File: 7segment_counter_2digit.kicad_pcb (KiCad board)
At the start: 2 copper layers, 68.6 x 94 mm, 14 parts, among them IC1 CD4026BE, IC2 CD4026BE, SW1 SW_Reset, SW2 SW_Count, U1 5611AH, U2 2462, U3 ICM7555, U4 5611AH

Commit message: Copy parts into project and fix library references
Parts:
- IC1, IC2: footprint SamacSys_Parts:DIP794W53P254L1930H508Q16N -> 7segment_counter:DIP794W53P254L1930H508Q16N
- SW1, SW2: footprint SamacSys_Parts:MJTP1212 -> 7segment_counter:MJTP1212
- U3: footprint SamacSys_Parts:DIP762W56P254L959H533Q8N -> 7segment_counter:DIP762W56P254L959H533Q8N

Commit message: Fix switches
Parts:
- removed SW1: SW_Reset, 7segment_counter:MJTP1212
- removed SW2: SW_Count, 7segment_counter:MJTP1212
- added SW_COUNT1: SW_Push_Dual, 7segment_counter:MJTP1212, F.Cu at (135.1, 111.5)
- added SW_RESET1: SW_Push_Dual, 7segment_counter:MJTP1212, F.Cu at (106.4, 111.5)
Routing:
- net VCC: track 176.1 -> 161.9 mm
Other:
- board text added: "v02"
- board text removed: "v01"

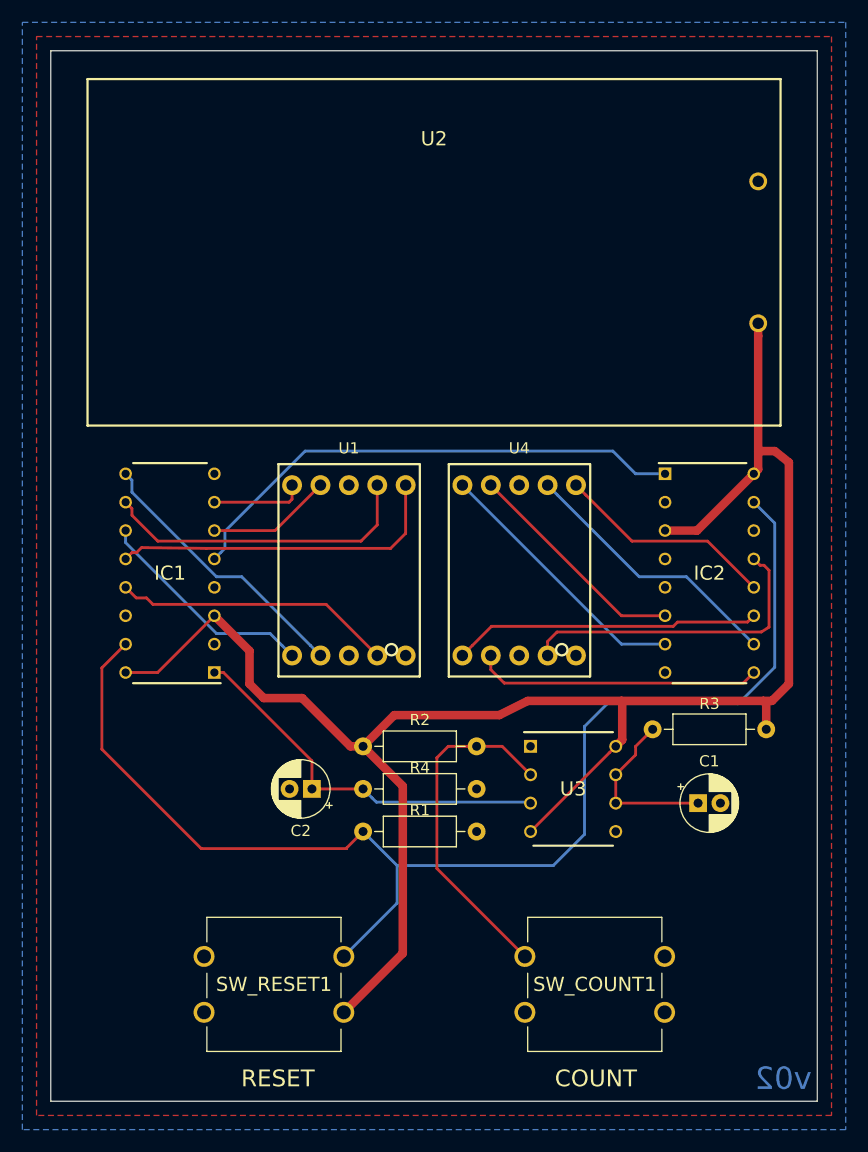
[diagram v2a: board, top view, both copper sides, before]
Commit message: Fix battery holder dimensions and digit positions
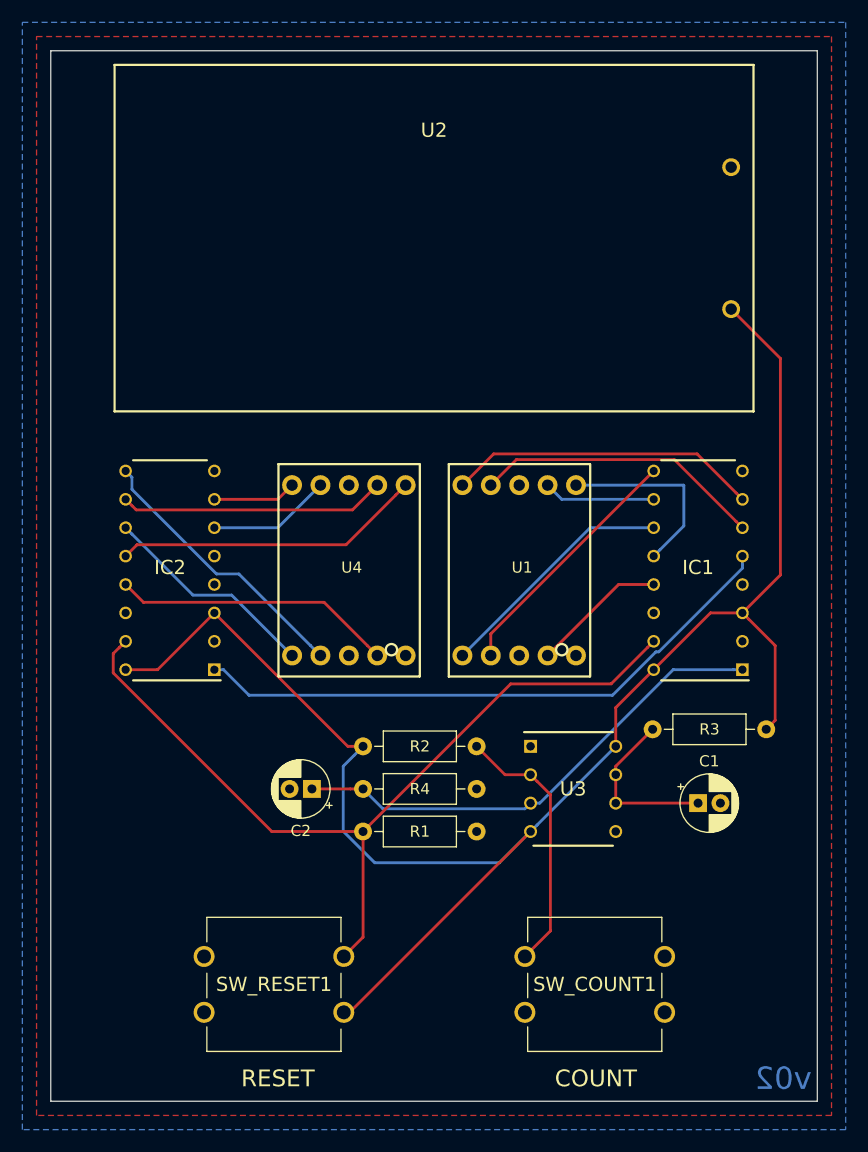
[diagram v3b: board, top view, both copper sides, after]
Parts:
- moved IC2 48.3 mm to (103.4, 77.0), turned to 180 degrees
- moved IC1 47.2 mm to (150.6, 77.0)
- moved U1 15.2 mm to (134.6, 77.0)
- moved U4 15.2 mm to (119.4, 77.0)
- moved U2 1.27 mm to (127.0, 47.2)
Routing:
- net Net-(IC1-Pad15): track 114.7 -> 76.5 mm
- net Net-(IC1-Pad7): track 8.32 -> 27.9 mm
- net Net-(IC1-Pad10): track 28.5 -> 10.0 mm
- net Net-(IC2-Pad7): track 24.0 -> 7.48 mm
- net Net-(IC1-Pad6): track 11.2 -> 26.0 mm
- net Net-(IC1-Pad12): track 30.3 -> 17.1 mm
- net Net-(IC1-Pad13): track 25.0 -> 12.1 mm
- net VCC: track 161.9 -> 150.6 mm
- net Net-(C2-Pad1): track 34.6 -> 44.4 mm
- net Net-(IC2-Pad6): track 20.4 -> 11.1 mm
- net Net-(IC2-Pad12): track 19.7 -> 27.7 mm
- net Net-(IC1-Pad5): track 46.1 -> 54.0 mm
- net Net-(IC2-Pad11): track 27.5 -> 19.6 mm
- net Net-(R2-Pad2): track 30.9 -> 23.8 mm
- net Net-(IC2-Pad13): track 28.4 -> 25.1 mm
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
